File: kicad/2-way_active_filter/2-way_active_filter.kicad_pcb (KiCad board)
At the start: 2 copper layers, 112 x 109.6 mm, 147 parts

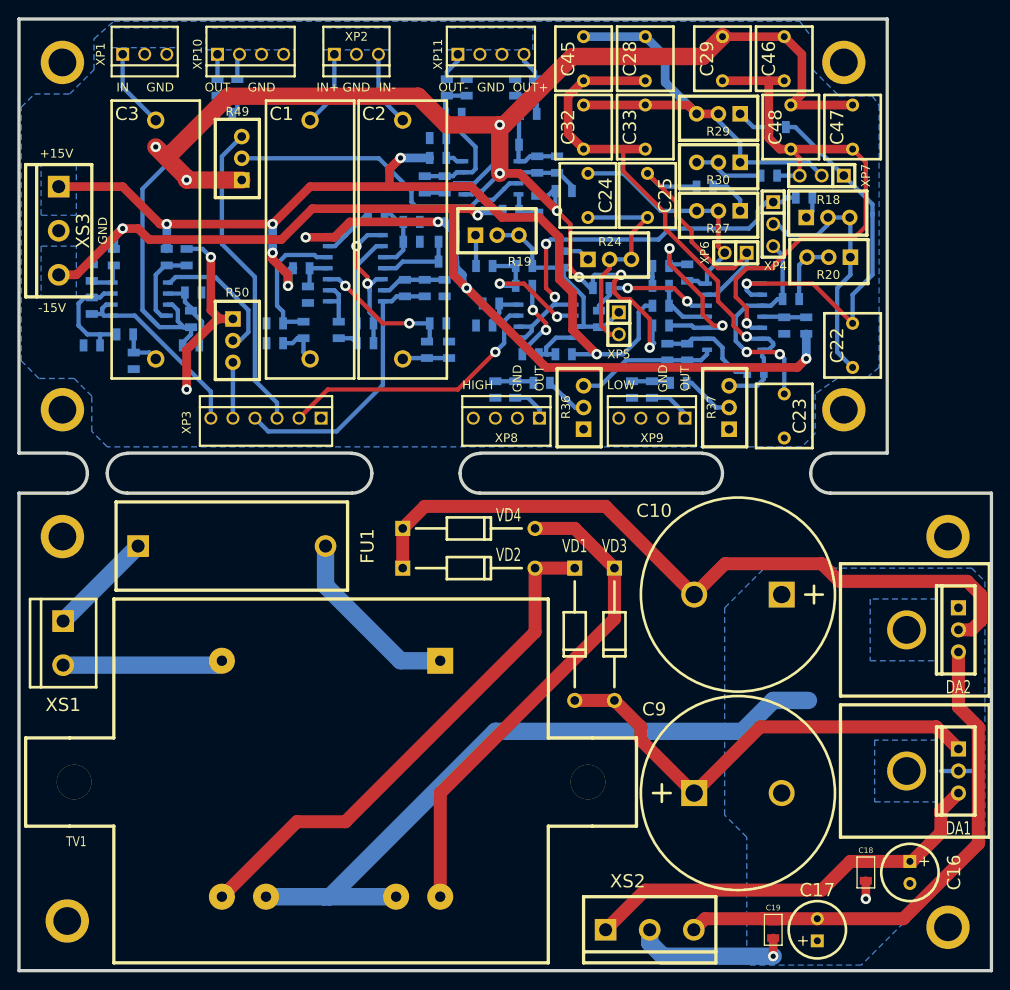
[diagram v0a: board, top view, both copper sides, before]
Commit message: Moved to kicad 4.0.0
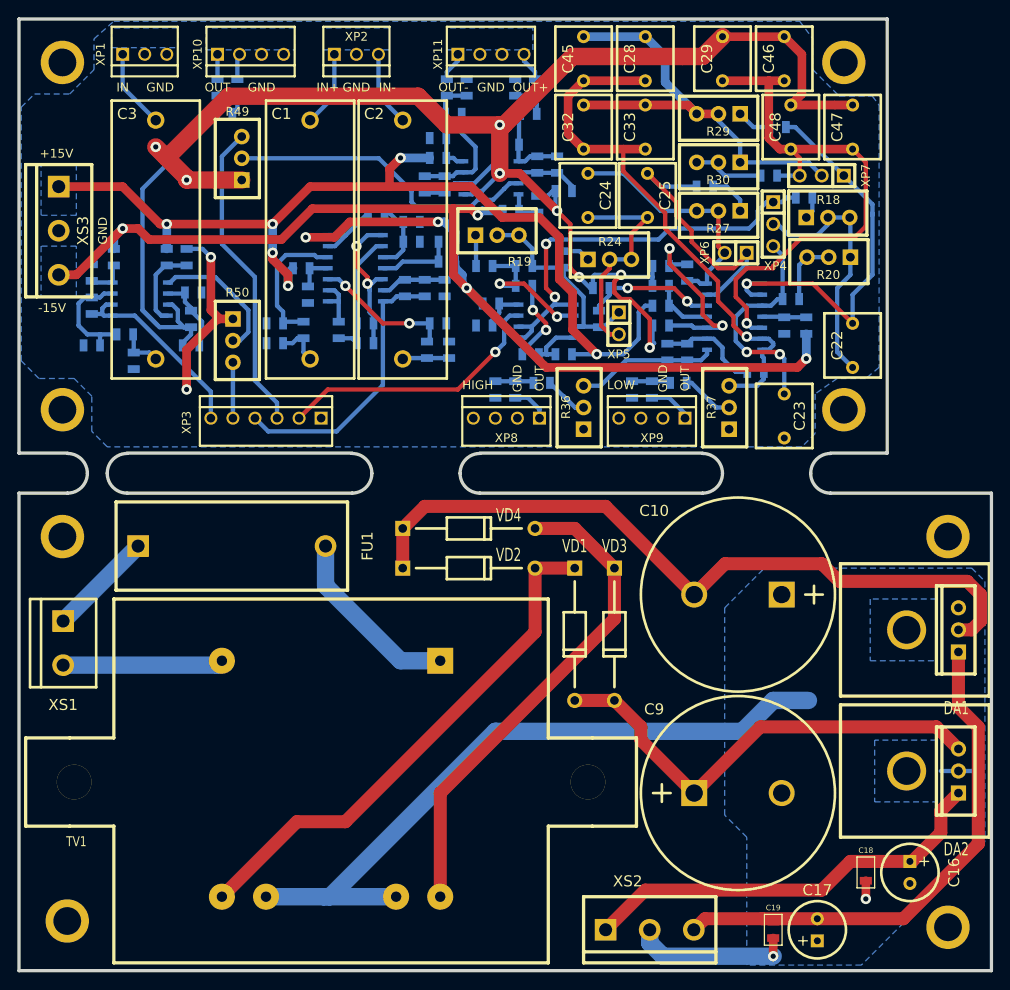
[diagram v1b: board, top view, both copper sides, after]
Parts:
- DA1, DA2: footprint TO220_RAD_16.5x15 -> LFcomponents:TO220_RAD_16.5x15
- moved DA1 17.3 mm to (190.9, 111.8), turned to 180 degrees
- moved DA2 17.3 mm to (190.9, 128.0), turned to 180 degrees
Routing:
- net Net-(C9-Pad1): track 53.7 -> 73.2 mm
- net Net-(C17-Pad2): track 61.3 -> 41.9 mm
- net Net-(C16-Pad1): track 50.7 -> 45.3 mm
- net /AGND: track 104.9 -> 109.2 mm
- net Net-(C10-Pad2): track 85.4 -> 86.5 mm
